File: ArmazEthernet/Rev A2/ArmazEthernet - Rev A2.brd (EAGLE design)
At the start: 72 x 80 mm, 140 parts, among them J1 22-05-7028-02, P1 RB1-125BAG1A, U1 LM317MDCY, U2 LM317MDCY, U3 KSZ8995MA, U4 AT24C02C-SSHM-B, X1 NE8FAV, X2 NE8FAV, Y1 8Z-25.000MHZMAAJ-T

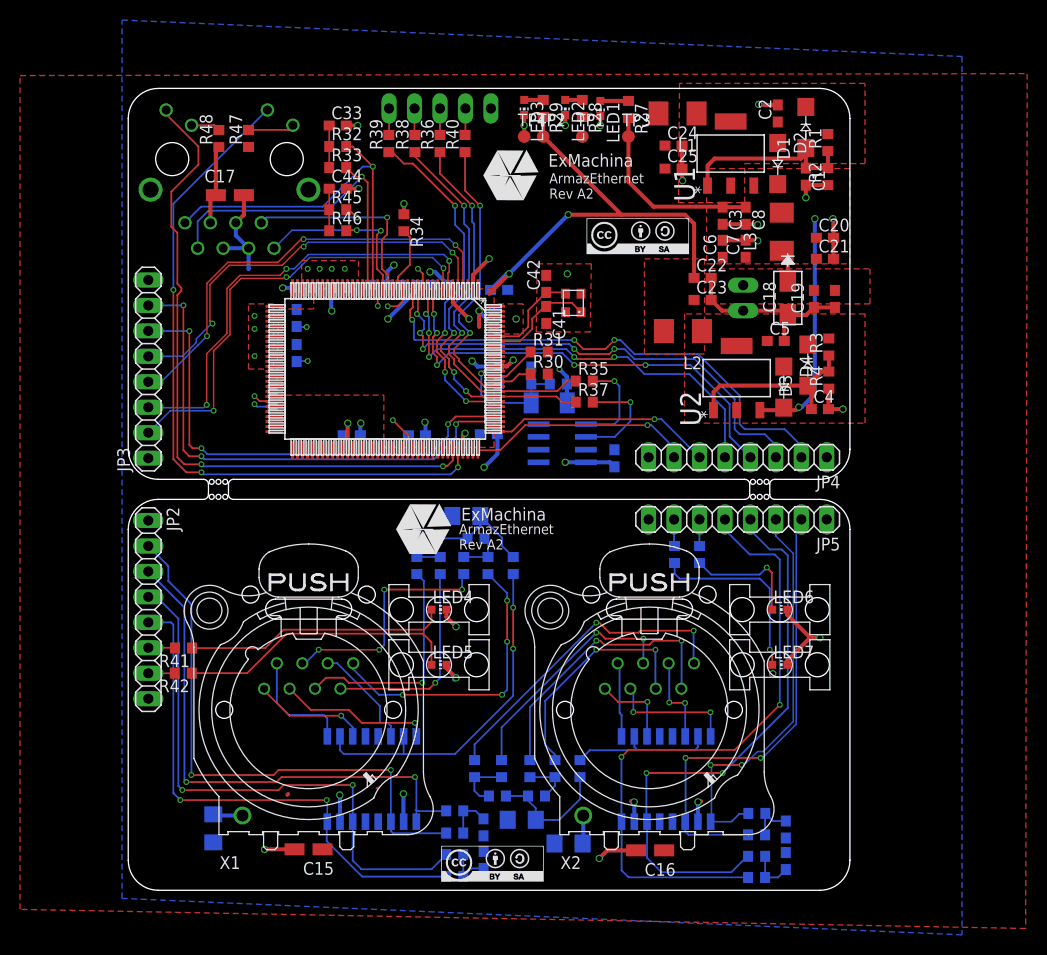
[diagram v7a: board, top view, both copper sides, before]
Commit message: Update the route of the board and the schematic
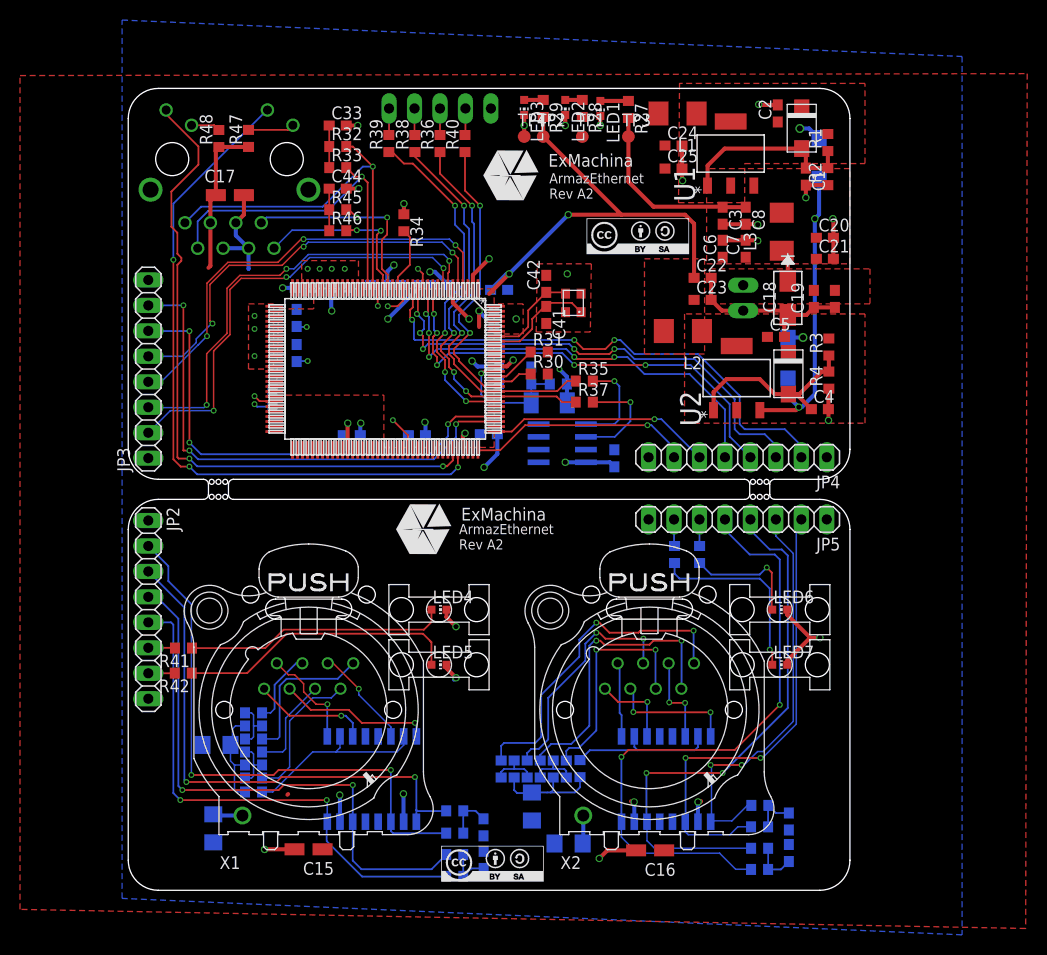
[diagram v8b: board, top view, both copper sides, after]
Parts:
- removed D1, D2, D3, D4: GF1, diode:SMA-DO214AC
- added U$11, U$12, U$13, U$7: GF1A, diode:DO-214BA
- C16, C17: value 4.78uF -> 4.7uF
- C19, C21: value 10uF -> 0.1uF
- L1, L2, L3: value 15uH_3A_20% -> 15uH_10%
- moved R6 34.4 mm to (12.5, 9.81), turned to 180 degrees
- moved C12 33.8 mm to (8.80, 14.5)
- moved R5 29.1 mm to (12.5, 15.1), turned to 180 degrees
- moved R10 29.0 mm to (12.5, 16.4)
- moved R18 28.6 mm to (12.5, 12.5), turned to 180 degrees
- moved R8 28.2 mm to (12.5, 11.2), turned to 180 degrees
- moved R11 25.6 mm to (12.5, 17.7), turned to 180 degrees
- moved R17 24.7 mm to (12.5, 13.8), turned to 180 degrees
- moved R15 3.17 mm to (42.4, 12.1), turned to 90 degrees
- moved R7 3.17 mm to (38.5, 12.1), turned to 90 degrees
- moved R9 2.65 mm to (37.2, 12.1)
- moved R16 2.56 mm to (39.8, 12.1)
- moved C11 1.67 mm to (40.3, 8.36), turned to 270 degrees
- moved R14 1.12 mm to (43.7, 12.1)
- moved R12 1.03 mm to (41.1, 12.1)
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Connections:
- net +1V8/FIL: now also U$12.C, U$13.A; no longer D3.K, D4.A
- net +3V3/FIL: now also U$11.C, U$7.A; no longer D1.K, D2.A
- net +5V: now also U$13.C, U$7.C; no longer D2.K, D4.K
- net N$2: now also U$11.A; no longer D1.A
- net N$6: now also U$12.A; no longer D3.A
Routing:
- net N$1: track 35.1 -> 18.7 mm, vias 2 -> 0
- net N$7: track 23.8 -> 7.47 mm, vias 4 -> 0
- net N$8: track 29.6 -> 15.2 mm, vias 4 -> 0
- net N$11: track 22.6 -> 9.70 mm, vias 1 -> 0
- net +3V3: track 40.0 -> 47.3 mm
- net +5V: track 43.1 -> 50.1 mm
- net N$9: track 20.8 -> 14.2 mm, vias 1 -> 0
- net +3V3/FIL: track 0.00 -> 2.33 mm, vias 0 -> 1
- net RX2_ISO_P: track 104.3 -> 102.0 mm
- net RX2_ISO_N: track 109.1 -> 107.1 mm
- net N$6: track 18.2 -> 19.9 mm
- net N$13: track 12.4 -> 10.8 mm
- net +1V8/FIL: track 0.00 -> 1.55 mm, vias 0 -> 1
- net N$32: track 11.2 -> 9.84 mm
- net RX1_M: track 11.4 -> 10.4 mm, vias 0 -> 1
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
